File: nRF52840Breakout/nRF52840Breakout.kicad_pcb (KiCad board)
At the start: 4 copper layers, 30.9 x 25 mm, 36 parts, among them J1 Conn_01x20_Female, J2 Conn_01x20_Female, J3 Conn_01x20_Female, SW1 SW_Push, U1 nRF52840, X1 Crystal, X2 32.768kHz

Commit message: keyboard schematic with breakout
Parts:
- renumbered REF** to REF**1, REF** to REF**2
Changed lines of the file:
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@@
     )
     (pad "1" thru_hole rect (at 0 0) (size 0.8 0.6) (drill 0.4) (layers *.Cu *.Mask)
-      (net 54 "Net-(J3-Pad1)") (pinfunction "Pin_1") (pintype "passive"))
+      (net 54 "Net-(J3-Pad1)") (pinfunction "Pin_1"))
     (pad "2" thru_hole rect (at 0 1) (size 0.8 0.6) (drill 0.4) (layers *.Cu *.Mask)
-      (net 55 "Net-(J3-Pad2)") (pinfunction "Pin_2") (pintype "passive"))
+      (net 55 "Net-(J3-Pad2)") (pinfunction "Pin_2"))
     (pad "3" thru_hole rect (at 0 2) (size 0.8 0.6) (drill 0.4) (layers *.Cu *.Mask)
-      (net 58 "Net-(J3-Pad3)") (pinfunction "Pin_3") (pintype "passive"))
+      (net 58 "Net-(J3-Pad3)") (pinfunction "Pin_3"))
     (pad "4" thru_hole rect (at 0 3) (size 0.8 0.6) (drill 0.4) (layers *.Cu *.Mask)
-      (net 59 "Net-(J3-Pad4)") (pinfunction "Pin_4") (pintype "passive"))
+      (net 59 "Net-(J3-Pad4)") (pinfunction "Pin_4"))
     (pad "5" thru_hole rect (at 0 4) (size 0.8 0.6) (drill 0.4) (layers *.Cu *.Mask)
-      (net 60 "Net-(J3-Pad5)") (pinfunction "Pin_5") (pintype "passive"))
+      (net 60 "Net-(J3-Pad5)") (pinfunction "Pin_5"))
     (pad "6" thru_hole rect (at 0 5) (size 0.8 0.6) (drill 0.4) (layers *.Cu *.Mask)
-      (net 61 "Net-(J3-Pad6)") (pinfunction "Pin_6") (pintype "passive"))
+      (net 61 "Net-(J3-Pad6)") (pinfunction "Pin_6"))
     (pad "7" thru_hole rect (at 0 6) (size 0.8 0.6) (drill 0.4) (layers *.Cu *.Mask)
-      (net 62 "Net-(J3-Pad7)") (pinfunction "Pin_7") (pintype "passive"))
+      (net 62 "Net-(J3-Pad7)") (pinfunction "Pin_7"))
     (pad "8" thru_hole rect (at 0 7) (size 0.8 0.6) (drill 0.4) (layers *.Cu *.Mask)
-      (net 63 "Net-(J3-Pad8)") (pinfunction "Pin_8") (pintype "passive"))
+      (net 63 "Net-(J3-Pad8)") (pinfunction "Pin_8"))
     (pad "9" thru_hole rect (at 0 8) (size 0.8 0.6) (drill 0.4) (layers *.Cu *.Mask)
-      (net 64 "Net-(J3-Pad9)") (pinfunction "Pin_9") (pintype "passive"))
+      (net 64 "Net-(J3-Pad9)") (pinfunction "Pin_9"))
     (pad "10" thru_hole rect (at 0 9) (size 0.8 0.6) (drill 0.4) (layers *.Cu *.Mask)
-      (net 3 "GND") (pinfunction "Pin_10") (pintype "passive"))
+      (net 3 "GND") (pinfunction "Pin_10"))
     (pad "11" thru_hole rect (at 0 10) (size 0.8 0.6) (drill 0.4) (layers *.Cu *.Mask)
-      (net 7 "VDD") (pinfunction "Pin_11") (pintype "passive"))
+      (net 7 "VDD") (pinfunction "Pin_11"))
     (pad "12" thru_hole rect (at 0 11) (size 0.8 0.6) (drill 0.4) (layers *.Cu *.Mask)
-      (net 56 "VDDH") (pinfunction "Pin_12") (pintype "passive"))
+      (net 56 "VDDH") (pinfunction "Pin_12"))
     (pad "13" thru_hole rect (at 0 12) (size 0.8 0.6) (drill 0.4) (layers *.Cu *.Mask)
-      (net 65 "Net-(J3-Pad13)") (pinfunction "Pin_13") (pintype "passive"))
+      (net 65 "Net-(J3-Pad13)") (pinfunction "Pin_13"))
     (pad "14" thru_hole rect (at 0 13) (size 0.8 0.6) (drill 0.4) (layers *.Cu *.Mask)
-      (net 66 "Net-(J3-Pad14)") (pinfunction "Pin_14") (pintype "passive"))
+      (net 66 "Net-(J3-Pad14)") (pinfunction "Pin_14"))
     (pad "15" thru_hole rect (at 0 14) (size 0.8 0.6) (drill 0.4) (layers *.Cu *.Mask)
-      (net 67 "Net-(J3-Pad15)") (pinfunction "Pin_15") (pintype "passive"))
+      (net 67 "Net-(J3-Pad15)") (pinfunction "Pin_15"))
     (pad "16" thru_hole rect (at 0 15) (size 0.8 0.6) (drill 0.4) (layers *.Cu *.Mask)
-      (net 68 "Net-(J3-Pad16)") (pinfunction "Pin_16") (pintype "passive"))
+      (net 68 "Net-(J3-Pad16)") (pinfunction "Pin_16"))
     (pad "17" thru_hole rect (at 0 16) (size 0.8 0.6) (drill 0.4) (layers *.Cu *.Mask)
-      (net 69 "Net-(J3-Pad17)") (pinfunction "Pin_17") (pintype "passive"))
+      (net 69 "Net-(J3-Pad17)") (pinfunction "Pin_17"))
     (pad "18" thru_hole rect (at 0 17) (size 0.8 0.6) (drill 0.4) (layers *.Cu *.Mask)
-      (net 70 "Net-(J3-Pad18)") (pinfunction "Pin_18") (pintype "passive"))
+      (net 70 "Net-(J3-Pad18)") (pinfunction "Pin_18"))
     (pad "19" thru_hole rect (at 0 18) (size 0.8 0.6) (drill 0.4) (layers *.Cu *.Mask)
-      (net 18 "USB_D+") (pinfunction "Pin_19") (pintype "passive"))
+      (net 18 "USB_D+") (pinfunction "Pin_19"))
     (pad "20" thru_hole rect (at 0 19) (size 0.8 0.6) (drill 0.4) (layers *.Cu *.Mask)
-      (net 17 "USB_D-") (pinfunction "Pin_20") (pintype "passive"))
+      (net 17 "USB_D-") (pinfunction "Pin_20"))
   )
   (footprint "Capacitor_SMD:C_0402_1005Metric_Pad0.74x0.62mm_HandSolder" (layer "F.Cu")
@@
     (tags "mounting hole 2.1mm no annular")
     (attr exclude_from_pos_files exclude_from_bom)
-    (fp_text reference "REF**" (at 0 -3.2) (layer "F.SilkS") hide
+    (fp_text reference "REF**2" (at 0 -3.2) (layer "F.SilkS") hide
       (effects (font (size 1 1) (thickness 0.15)))
     )
@@
     (tags "mounting hole 2.1mm no annular")
     (attr exclude_from_pos_files exclude_from_bom)
-    (fp_text reference "REF**" (at 0 -3.2) (layer "F.SilkS") hide
-      (effects (font (size 1 1) (thickness 0.15)))
-    )
+    (fp_text reference "REF**1" (at 0 -3.2) (layer "F.SilkS") hide
+      (effects (font (size 1 1) (thickness 0.15)))
+    )

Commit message: update breakout without castellations
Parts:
- moved AE1 23.5 mm to (22.9, 20.5)
- moved C1 23.5 mm to (28.9, 20.8)
- moved C11 23.5 mm to (31.8, 22.3)
- moved C12 23.5 mm to (31.0, 24.8)
- moved C14 23.5 mm to (29.9, 33.9)
- moved C18 23.5 mm to (34.9, 38.0)
- moved C19 23.5 mm to (36.7, 32.4)
- moved C20 23.5 mm to (42.3, 34.3)
- moved C21 23.5 mm to (40.5, 31.4)
- moved C3 23.5 mm to (24.8, 19.3)
- moved C6 23.5 mm to (38.0, 38.0)
- moved C8 23.5 mm to (40.8, 24.0)
- moved L1 23.5 mm to (24.7, 20.5)
- moved L4 23.5 mm to (37.3, 35.1)
- moved REF**1 23.5 mm to (18.2, 40.1)
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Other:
- board size 30.9 x 25 mm -> 31.6 x 26.4 mm

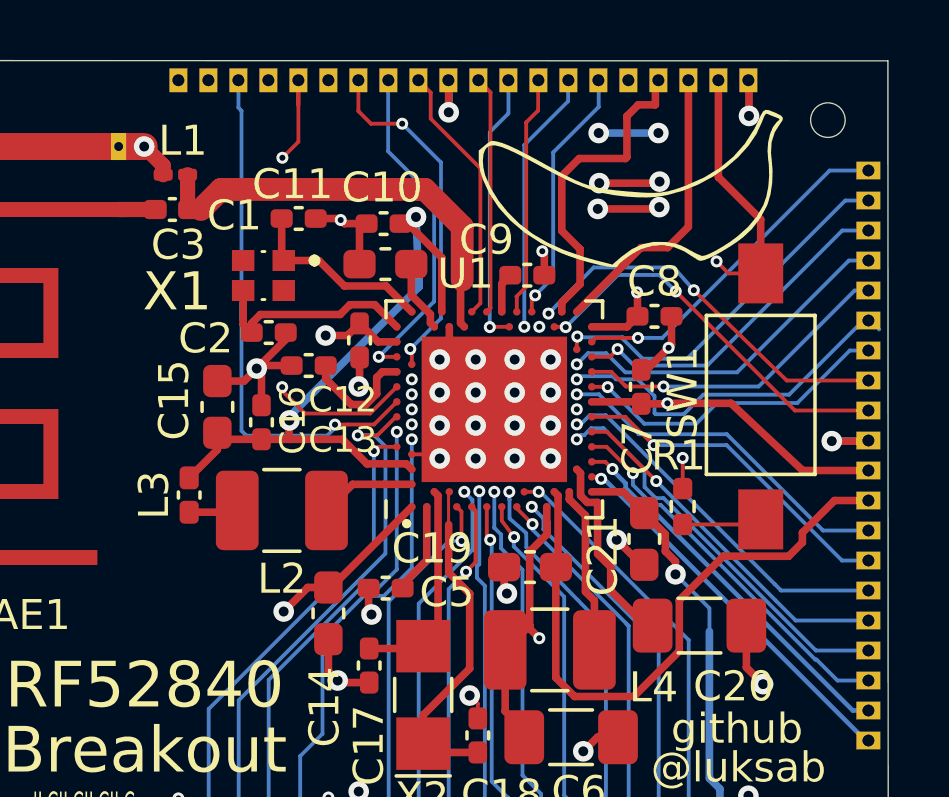
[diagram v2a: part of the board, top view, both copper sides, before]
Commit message: finish up Schematics
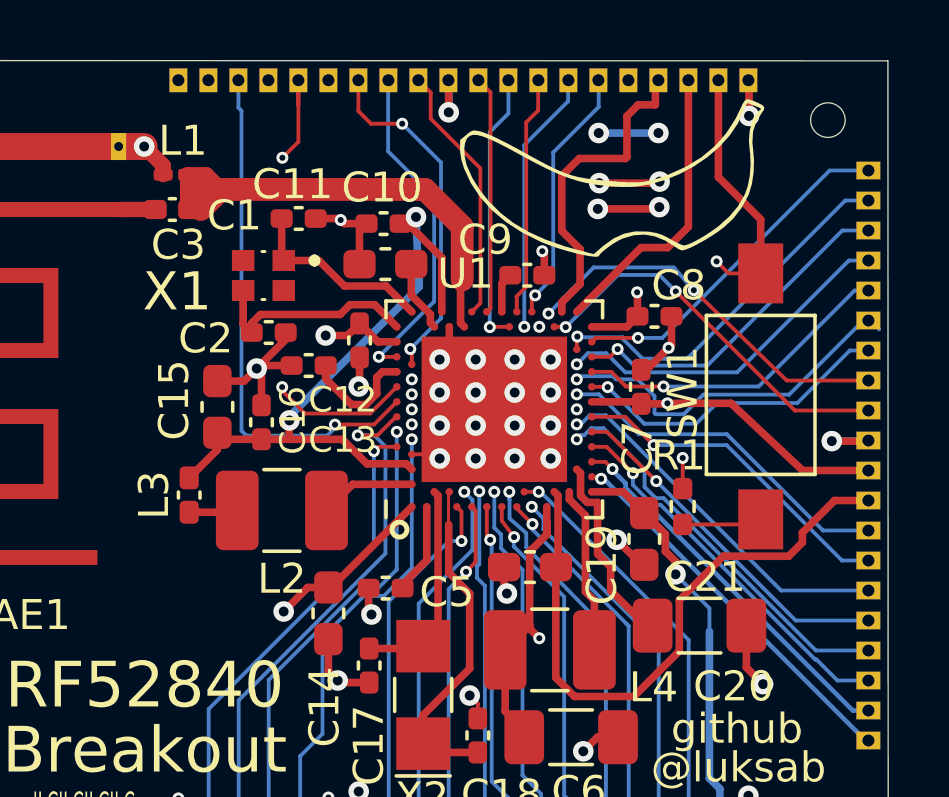
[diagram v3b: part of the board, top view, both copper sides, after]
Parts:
- moved G*** 0.71 mm to (39.3, 19.2)
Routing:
- net Net-(C3-Pad1): track 14.5 -> 17.8 mm
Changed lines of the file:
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@@
     (property "Sheetname" "")
     (attr smd)
-    (fp_text reference "C21" (at -0.56 -1.38 90) (layer "F.SilkS")
+    (fp_text reference "C21" (at -1.27 2.03 180) (layer "F.SilkS")
       (effects (font (size 1 1) (thickness 0.15)))
     )
@@
   )
   (footprint "LOGO" (layer "F.Cu")
-    (at 39.915893 19.562212 -95)
+    (at 39.295893 19.212212 -95)
     (attr board_only exclude_from_pos_files exclude_from_bom)
     (fp_text reference "G***" (at -2.08 1.41 -5) (layer "F.SilkS") hide
@@
     (property "Sheetname" "")
     (attr smd)
-    (fp_text reference "C9" (at -1.36 -1.18) (layer "F.SilkS")
+    (fp_text reference "C9" (at -1.4 -1.18) (layer "F.SilkS")
       (effects (font (size 1 1) (thickness 0.15)))
     )
@@
     (property "Sheetname" "")
     (attr smd)
-    (fp_text reference "C19" (at -3.26 -0.62) (layer "F.SilkS")
+    (fp_text reference "C19" (at 2.4 -0.08 90) (layer "F.SilkS")
       (effects (font (size 1 1) (thickness 0.15)))
     )
@@
     (fp_line (start -0.8 0.4) (end -0.8 -0.4) (layer "F.Fab") (width 0.1))
     (pad "1" smd roundrect (at -0.8625 0) (locked) (size 1.075 0.95) (layers "F.Cu" "F.Paste" "F.Mask") (roundrect_rratio 0.25)
-      (net 3 "GND") (pintype "passive"))
+      (net 3 "GND"))
     (pad "2" smd roundrect (at 0.8625 0) (locked) (size 1.075 0.95) (layers "F.Cu" "F.Paste" "F.Mask") (roundrect_rratio 0.25)
-      (net 56 "VDDH") (pintype "passive"))
+      (net 56 "VDDH"))
     (model "${KICAD6_3DMODEL_DIR}/Capacitor_SMD.3dshapes/C_0603_1608Metric.wrl"
       (offset (xyz 0 0 0))
@@
     (property "Sheetname" "")
     (attr smd)
-    (fp_text reference "C8" (at 0 -1.16) (layer "F.SilkS")
+    (fp_text reference "C8" (at 0.81 -1.03) (layer "F.SilkS")
       (effects (font (size 1 1) (thickness 0.15)))
     )
@@
     )
   )
-  (gr_circle (center 32.55 30.93) (end 32.62 30.97) (layer "F.SilkS") (width 0.1524) (fill none))
+  (gr_circle (center 32.31 31.13) (end 32.39 31.15) (layer "F.SilkS") (width 0.5) (fill none))
   (gr_line (start 17.04 15.495) (end 17.05 41.9) (layer "Edge.Cuts") (width 0.0381))
   (gr_line (start 48.6 41.9) (end 48.59 15.505) (layer "Edge.Cuts") (width 0.0381))
@@
   (segment (start 27.1 24.2775) (end 27.3825 24.56) (width 0.254) (layer "F.Cu") (net 4))
   (segment (start 26.36 19.79) (end 25.69 20.46) (width 0.762) (layer "F.Cu") (net 5))
+  (segment (start 25.2475 19.3) (end 25.87 19.3) (width 0.508) (layer "F.Cu") (net 5))
   (segment (start 34.345 24.245) (end 34.345 22.865) (width 0.254) (layer "F.Cu") (net 5))
   (segment (start 33.03 19.79) (end 33.159389 19.79) (width 0.762) (layer "F.Cu") (net 5))
+  (segment (start 25.87 19.3) (end 26.36 19.79) (width 0.508) (layer "F.Cu") (net 5))
   (segment (start 25.69 20.46) (end 25.3125 20.46) (width 0.254) (layer "F.Cu") (net 5))
   (segment (start 25.2475 20.395) (end 25.3125 20.46) (width 0.254) (layer "F.Cu") (net 5))
   (segment (start 34.47 24.37) (end 34.345 24.245) (width 0.254) (layer "F.Cu") (net 5))
   (segment (start 34.4 21.030611) (end 34.4 22.81) (width 0.762) (layer "F.Cu") (net 5))
-  (segment (start 25.2475 19.3) (end 25.2475 20.395) (width 0.508) (layer "F.Cu") (net 5))
   (segment (start 33.03 19.79) (end 26.36 19.79) (width 0.762) (layer "F.Cu") (net 5))
   (segment (start 33.159389 19.79) (end 34.4 21.030611) (width 0.762) (layer "F.Cu") (net 5))
+  (segment (start 25.2475 19.3) (end 25.2475 19.8075) (width 0.508) (layer "F.Cu") (net 5))
+  (segment (start 25.2475 19.8075) (end 25.8925 19.8075) (width 0.508) (layer "F.Cu") (net 5))
+  (segment (start 25.8925 19.8075) (end 25.8925 19.88) (width 0.508) (layer "F.Cu") (net 5))
+  (segment (start 25.8925 19.88) (end 25.3125 20.46) (width 0.508) (layer "F.Cu") (net 5))
+  (segment (start 26.3425 19.8075) (end 26.36 19.79) (width 0.508) (layer "F.Cu") (net 5))
   (segment (start 34.345 22.865) (end 34.4 22.81) (width 0.254) (layer "F.Cu") (net 5))
+  (segment (start 25.2475 19.8075) (end 25.2475 20.395) (width 0.508) (layer "F.Cu") (net 5))
+  (segment (start 25.8925 19.8075) (end 26.3425 19.8075) (width 0.508) (layer "F.Cu") (net 5))
   (segment (start 33.22 32.1475) (end 32.2875 33.08) (width 0.254) (layer "F.Cu") (net 6))
   (segment (start 33.22 30.37) (end 33.22 32.1475) (width 0.254) (layer "F.Cu") (net 6))
